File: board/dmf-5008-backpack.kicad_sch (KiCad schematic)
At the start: 24 parts

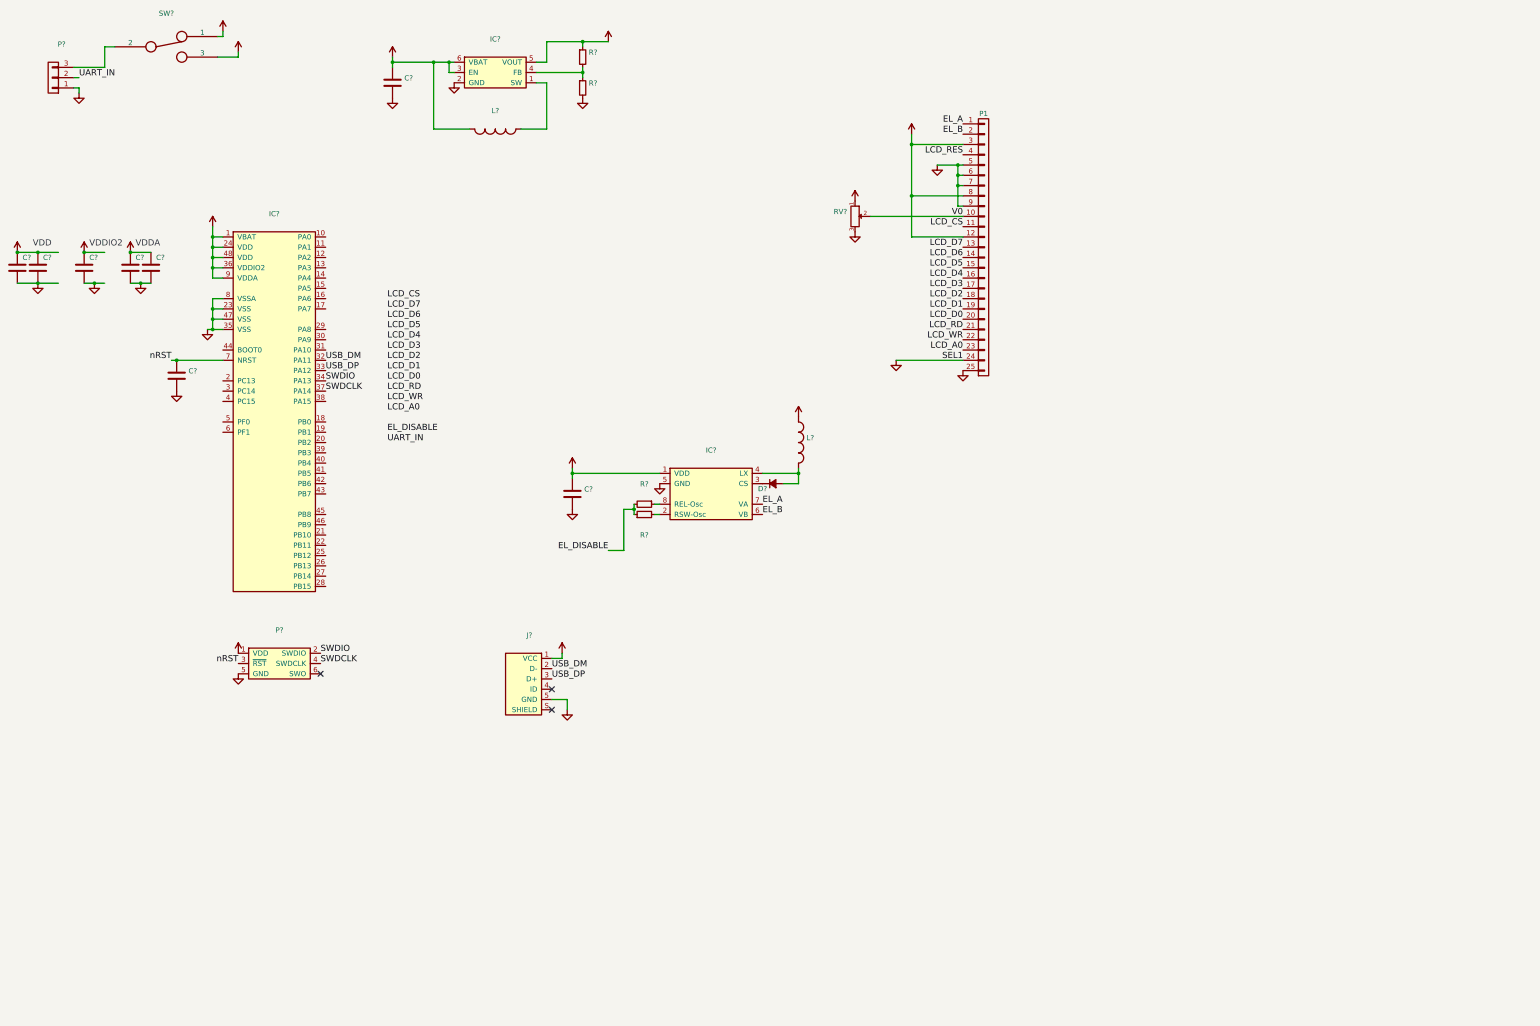
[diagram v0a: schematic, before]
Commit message: Rough draft of redesign around Pi Pico
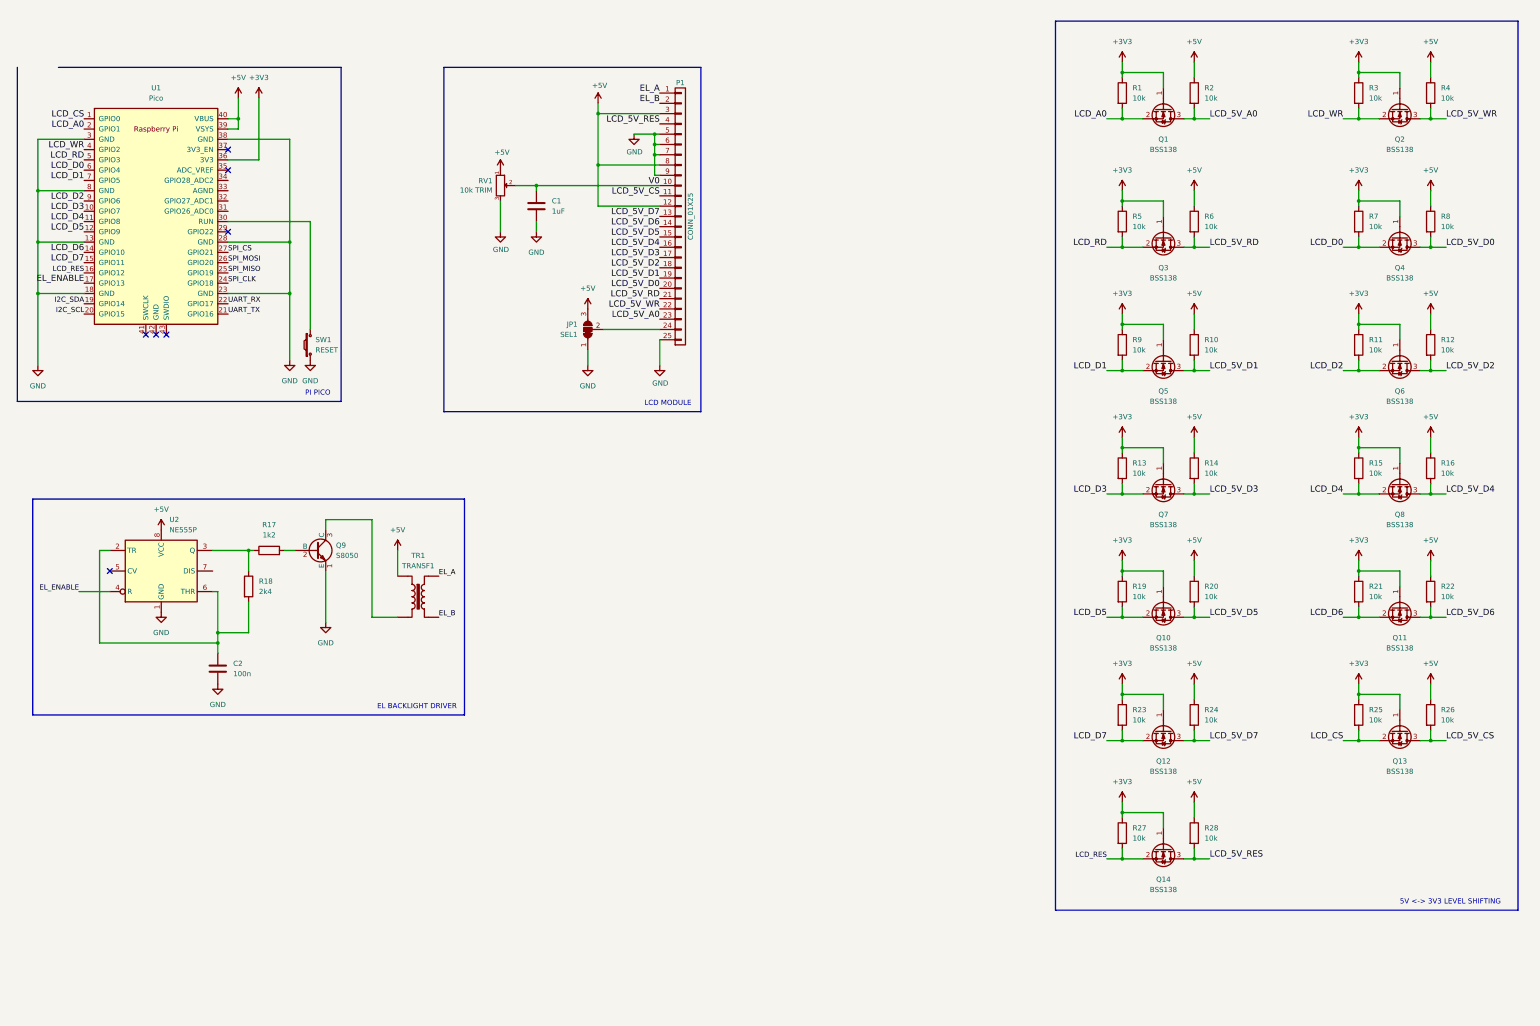
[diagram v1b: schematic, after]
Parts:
- removed C? (x8): (no value), symbol device:C
- removed D?: (no value), symbol device:D_Small
- removed IC?: (no value), symbol dmf-5008-backpack-rescue:TLV61220
- removed IC?: (no value), symbol dmf-5008-backpack-rescue:STM32F0xxCxTx
- removed IC?: (no value), symbol dmf-5008-backpack-rescue:HV823
- removed J?: (no value), symbol microusb:MICROUSB
- removed L? (x2): (no value), symbol device:INDUCTOR_SMALL
- removed P?: (no value), symbol conn:CONN_01X03
- removed P?: (no value), symbol swd_tc:SWD_TC
- removed R? (x4): (no value), symbol device:R_Small
- removed SW?: (no value), symbol device:SWITCH_INV
- added C1: 1uF, Capacitor_SMD:C_0805_2012Metric, symbol device:C
- added C2: 100n, Capacitor_SMD:C_0603_1608Metric, symbol device:C
- added JP1: SEL1, Jumper:SolderJumper-3_P1.3mm_Bridged12_RoundedPad1.0x1.5mm_NumberLabels, symbol Jumper:SolderJumper_3_Bridged12
- added Q1, Q10, Q11, Q12, Q13, Q14, Q2, Q3, Q4, Q5, Q6, Q7, Q8: BSS138, Package_TO_SOT_SMD:SOT-23, symbol Transistor_FET:BSS138
- added Q9: S8050, Package_TO_SOT_THT:TO-92, symbol transistors:S8050
- added R1, R10, R11, R12, R13, R14, R15, R16, R19, R2, R20, R21, R22, R23, R24, R25, R26, R27, R28, R3, R4, R5, R6, R7, R8, R9: 10k, Resistor_SMD:R_0603_1608Metric, symbol device:R
- added R17: 1k2, Resistor_SMD:R_0603_1608Metric, symbol device:R
- added R18: 2k4, Resistor_SMD:R_0603_1608Metric, symbol device:R
- added SW1: RESET, Button_Switch_THT:SW_PUSH_6mm, symbol device:SW_PUSH_SMALL_H
- added TR1: TRANSF1, EE14_xformer:EE14_XFORMER, symbol Transformer:TRANSF1
- added U1: Pico, rp:RPi_Pico_SMD_TH, symbol rp:Pico
- added U2: NE555P, Package_DIP:DIP-8_W7.62mm, symbol Timer:NE555P
- P1: value (none) -> CONN_01X25; footprint (none) -> footprints:lcd_full
- RV1: renamed from RV?; value (none) -> 10k TRIM; footprint (none) -> Potentiometer_THT:Potentiometer_Bourns_3386F_Vertical
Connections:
- net +3V3: now also Q1.1 (G), Q10.1 (G), Q11.1 (G), Q12.1 (G), Q13.1 (G), Q14.1 (G), Q2.1 (G), Q3.1 (G), Q4.1 (G), Q5.1 (G), Q6.1 (G), Q7.1 (G), Q8.1 (G), R1.1, R11.1, R13.1, R15.1, R19.1, R21.1, R23.1, R25.1, R27.1, R3.1, R5.1, R7.1, R9.1, U1.36 (3V3)
- net +5V: now also JP1.3 (B), R10.1, R12.1, R14.1, R16.1, R2.1, R20.1, R22.1, R24.1, R26.1, R28.1, R4.1, R6.1, R8.1, TR1.1, U1.39 (VSYS), U1.40 (VBUS), U2.8 (VCC)
- net EL_A: now also TR1.4
- net EL_B: now also TR1.3
- net GND: now also C1.2, C2.2, JP1.1 (A), Q9.1 (E), SW1.1, U1.13 (GND), U1.18 (GND), U1.23 (GND), U1.28 (GND), U1.3 (GND), U1.38 (GND), U1.8 (GND), U2.1 (GND); no longer P1.24 (P24)
- net LCD_A0: now also Q1.2 (S), R1.2, U1.2 (GPIO1); no longer P1.23 (P23)
- net LCD_CS: now also Q13.2 (S), R25.2, U1.1 (GPIO0); no longer P1.11 (P11)
- net LCD_D0: now also Q4.2 (S), R7.2, U1.6 (GPIO4); no longer P1.20 (P20)
- net LCD_D1: now also Q5.2 (S), R9.2, U1.7 (GPIO5); no longer P1.19 (P19)
- net LCD_D2: now also Q6.2 (S), R11.2, U1.9 (GPIO6); no longer P1.18 (P18)
- net LCD_D3: now also Q7.2 (S), R13.2, U1.10 (GPIO7); no longer P1.17 (P17)
- net LCD_D4: now also Q8.2 (S), R15.2, U1.11 (GPIO8); no longer P1.16 (P16)
- net LCD_D5: now also Q10.2 (S), R19.2, U1.12 (GPIO9); no longer P1.15 (P15)
- net LCD_D6: now also Q11.2 (S), R21.2, U1.14 (GPIO10); no longer P1.14 (P14)
- net LCD_D7: now also Q12.2 (S), R23.2, U1.15 (GPIO11); no longer P1.13 (P13)
- net LCD_RD: now also Q3.2 (S), R5.2, U1.5 (GPIO3); no longer P1.21 (P21)
- net LCD_RES: now also Q14.2 (S), R27.2, U1.16 (GPIO12); no longer P1.4 (P4)
- net LCD_WR: now also Q2.2 (S), R3.2, U1.4 (GPIO2); no longer P1.22 (P22)
- net V0: now also C1.1
- new net: JP1.2 (C), P1.24 (P24)
- new net: C2.1, R18.2, U2.2 (TR), U2.6 (THR)
- new net: R17.1, R18.1, U2.3 (Q)
- new net: Q9.2 (B), R17.2
- new net: Q9.3 (C), TR1.2
- new net: SW1.2, U1.30 (RUN)
- new net EL_ENABLE: U1.17 (GPIO13), U2.4 (R)
- new net I2C_SCL: U1.20 (GPIO15)
- new net I2C_SDA: U1.19 (GPIO14)
- new net LCD_5V_A0: P1.23 (P23), Q1.3 (D), R2.2
- new net LCD_5V_CS: P1.11 (P11), Q13.3 (D), R26.2
- new net LCD_5V_D0: P1.20 (P20), Q4.3 (D), R8.2
- new net LCD_5V_D1: P1.19 (P19), Q5.3 (D), R10.2
- new net LCD_5V_D2: P1.18 (P18), Q6.3 (D), R12.2
- new net LCD_5V_D3: P1.17 (P17), Q7.3 (D), R14.2
- new net LCD_5V_D4: P1.16 (P16), Q8.3 (D), R16.2
- new net LCD_5V_D5: P1.15 (P15), Q10.3 (D), R20.2
- new net LCD_5V_D6: P1.14 (P14), Q11.3 (D), R22.2
- new net LCD_5V_D7: P1.13 (P13), Q12.3 (D), R24.2
- new net LCD_5V_RD: P1.21 (P21), Q3.3 (D), R6.2
- new net LCD_5V_RES: P1.4 (P4), Q14.3 (D), R28.2
- new net LCD_5V_WR: P1.22 (P22), Q2.3 (D), R4.2
- new net SPI_CLK: U1.24 (GPIO18)
- new net SPI_CS: U1.27 (GPIO21)
- new net SPI_MISO: U1.25 (GPIO19)
- new net SPI_MOSI: U1.26 (GPIO20)
- new net UART_RX: U1.22 (GPIO17)
- new net UART_TX: U1.21 (GPIO16)
- no-connect marks 3 -> 7
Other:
- note added: "5V <-> 3V3 LEVEL SHIFTING"
- note added: "EL BACKLIGHT DRIVER"
- note added: "LCD MODULE"
- note added: "PI PICO"
- note removed: "VDD"
- note removed: "VDDA"
- note removed: "VDDIO2"
- moved on the sheet: P1, RV1

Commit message: Rework schematic around MIC4830 EL driver
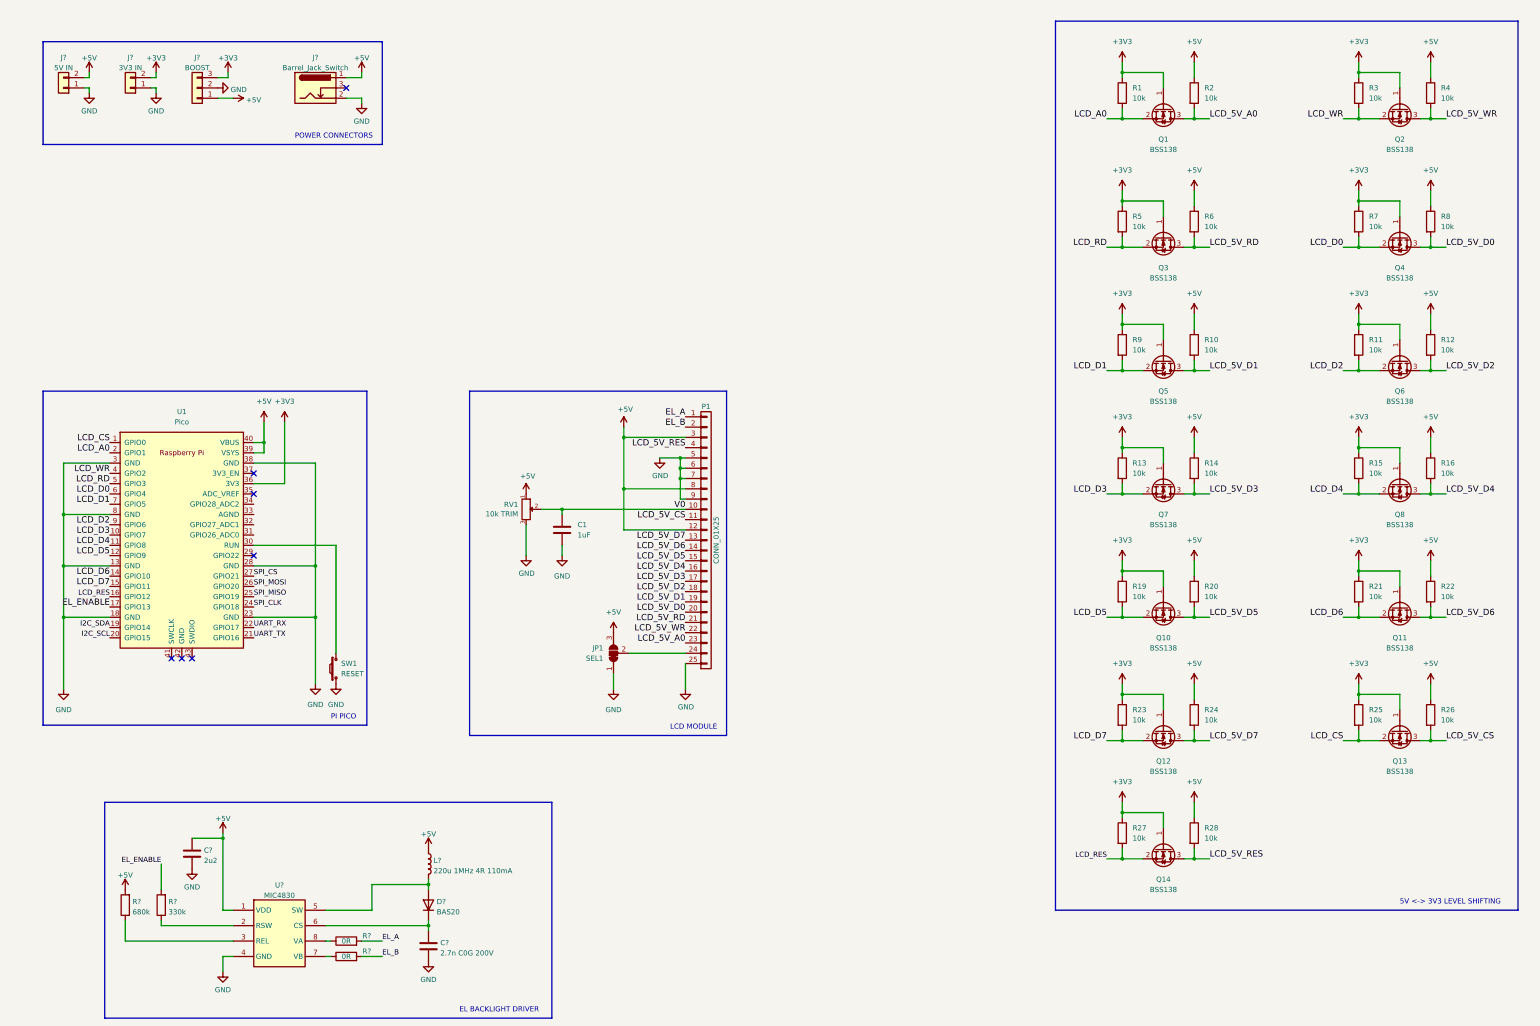
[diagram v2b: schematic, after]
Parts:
- removed C2: 100n, Capacitor_SMD:C_0603_1608Metric, symbol device:C
- removed Q9: S8050, Package_TO_SOT_THT:TO-92, symbol transistors:S8050
- removed R17: 1k2, Resistor_SMD:R_0603_1608Metric, symbol device:R
- removed R18: 2k4, Resistor_SMD:R_0603_1608Metric, symbol device:R
- removed TR1: TRANSF1, EE14_xformer:EE14_XFORMER, symbol Transformer:TRANSF1
- removed U2: NE555P, Package_DIP:DIP-8_W7.62mm, symbol Timer:NE555P
- added C?: 2u2, symbol Device:C
- added C?: 2.7n C0G 200V, Capacitor_SMD:C_0805_2012Metric_Pad1.18x1.45mm_HandSolder, symbol Device:C
- added D?: BAS20, Package_TO_SOT_SMD:SOT-23, symbol Diode:BAS20
- added J?: 5V IN, Connector_PinHeader_2.54mm:PinHeader_1x02_P2.54mm_Vertical, symbol Connector_Generic:Conn_01x02
- added J?: Barrel_Jack_Switch, symbol Connector:Barrel_Jack_Switch
- added J?: BOOST, Connector_PinHeader_2.54mm:PinHeader_1x03_P2.54mm_Vertical, symbol Connector_Generic:Conn_01x03
- added J?: 3V3 IN, Connector_PinHeader_2.54mm:PinHeader_1x02_P2.54mm_Vertical, symbol Connector_Generic:Conn_01x02
- added L?: 220u 1MHz 4R 110mA, symbol Device:L
- added R? (x2): 0R, Resistor_SMD:R_1206_3216Metric_Pad1.30x1.75mm_HandSolder, symbol Device:R
- added R?: 330k, Resistor_SMD:R_0603_1608Metric, symbol Device:R
- added R?: 680k, Resistor_SMD:R_0603_1608Metric, symbol Device:R
- added U?: MIC4830, Package_SO:MSOP-8_3x3mm_P0.65mm, symbol MIC4830:MIC4830
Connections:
- net +3V3: now also J?.2 (Pin_2), J?.3 (Pin_3)
- net +5V: now also C?.1, J?.1, J?.1 (Pin_1), J?.2 (Pin_2), L?.1, R?.2, U?.1 (VDD)
- net EL_A: now also R?.2
- net EL_B: now also R?.2
- net EL_ENABLE: now also R?.2
- net GND: now also C?.2, C?.2, J?.1 (Pin_1), J?.1 (Pin_1), J?.2, J?.2 (Pin_2), U?.4 (GND)
- new net: R?.1, U?.7 (VB)
- new net: R?.1, U?.2 (RSW)
- new net: R?.1, U?.3 (REL)
- new net: D?.1 (A), L?.2, U?.5 (SW)
- new net: C?.1, D?.3 (K), U?.6 (CS)
- new net: R?.1, U?.8 (VA)
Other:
- note added: "POWER CONNECTORS"
- moved on the sheet: C1, JP1, P1, RV1, SW1, U1

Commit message: Work on placement a bit
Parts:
- C2: renamed from C?; footprint (none) -> Capacitor_SMD:C_0805_2012Metric
- J4: renamed from J?; footprint (none) -> Connector_BarrelJack:BarrelJack_Horizontal
- gave numbers to parts that had none: 11
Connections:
- net RUN: now reaches SW1.2, U1.30 (RUN)
